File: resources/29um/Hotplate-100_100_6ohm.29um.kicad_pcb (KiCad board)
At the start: 2 copper layers, 100 x 100 mm, 7 parts, among them J1 Hotplate_Power_Connection, J2 Hotplate_Power_Connection

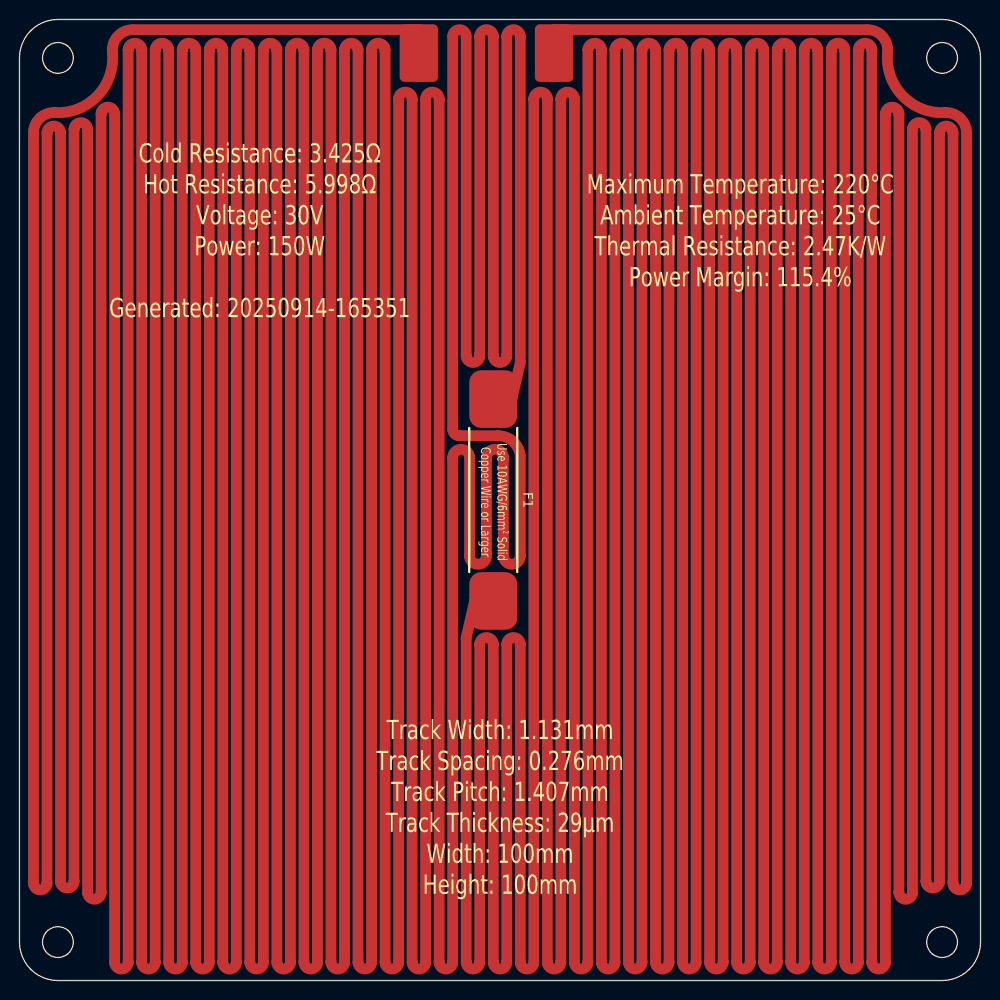
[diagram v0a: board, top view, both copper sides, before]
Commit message: Replaced obsolete 25mm thermal fuse footprint with new 35mm thermal fuse footprint.
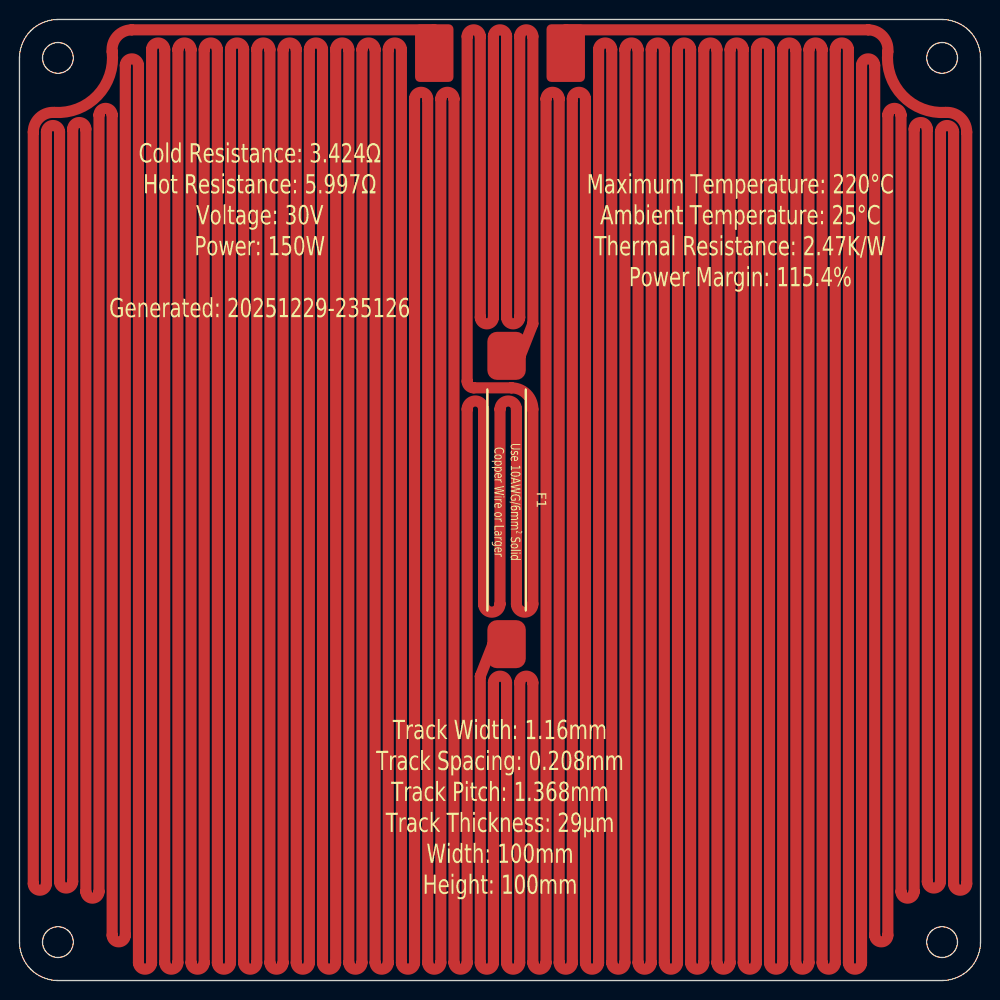
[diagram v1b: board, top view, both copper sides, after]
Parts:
- F1: footprint blg:Thermal Fuse, Front, 25mm -> blg:Thermal Fuse, SN100C, Front, 35mm
- moved J1 1.60 mm to (98.2, 58.5)
- moved F1 1.39 mm to (105.7, 105.0)
- moved J2 1.21 mm to (111.8, 58.5)
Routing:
- net Net-(J1-Pin_1): track 3264.0 -> 3469.5 mm
- net Net-(J2-Pin_1): track 3305.3 -> 3274.4 mm
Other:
- board text added: "Cold Resistance: 3.424Ω Hot Resistance: 5.997Ω Voltage: 30V Power: 150W Generated: 20251229-235126"
- board text added: "Track Width: 1.16mm Track Spacing: 0.208mm Track Pitch: 1.368mm Track Thickness: 29µm Width: 100mm Height: 100mm"
- board text removed: "Cold Resistance: 3.425Ω Hot Resistance: 5.998Ω Voltage: 30V Power: 150W Generated: 20250914-165351"
- board text removed: "Track Width: 1.131mm Track Spacing: 0.276mm Track Pitch: 1.407mm Track Thickness: 29µm Width: 100mm Height: 100mm"
